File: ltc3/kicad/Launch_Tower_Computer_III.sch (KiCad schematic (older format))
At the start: 0 parts

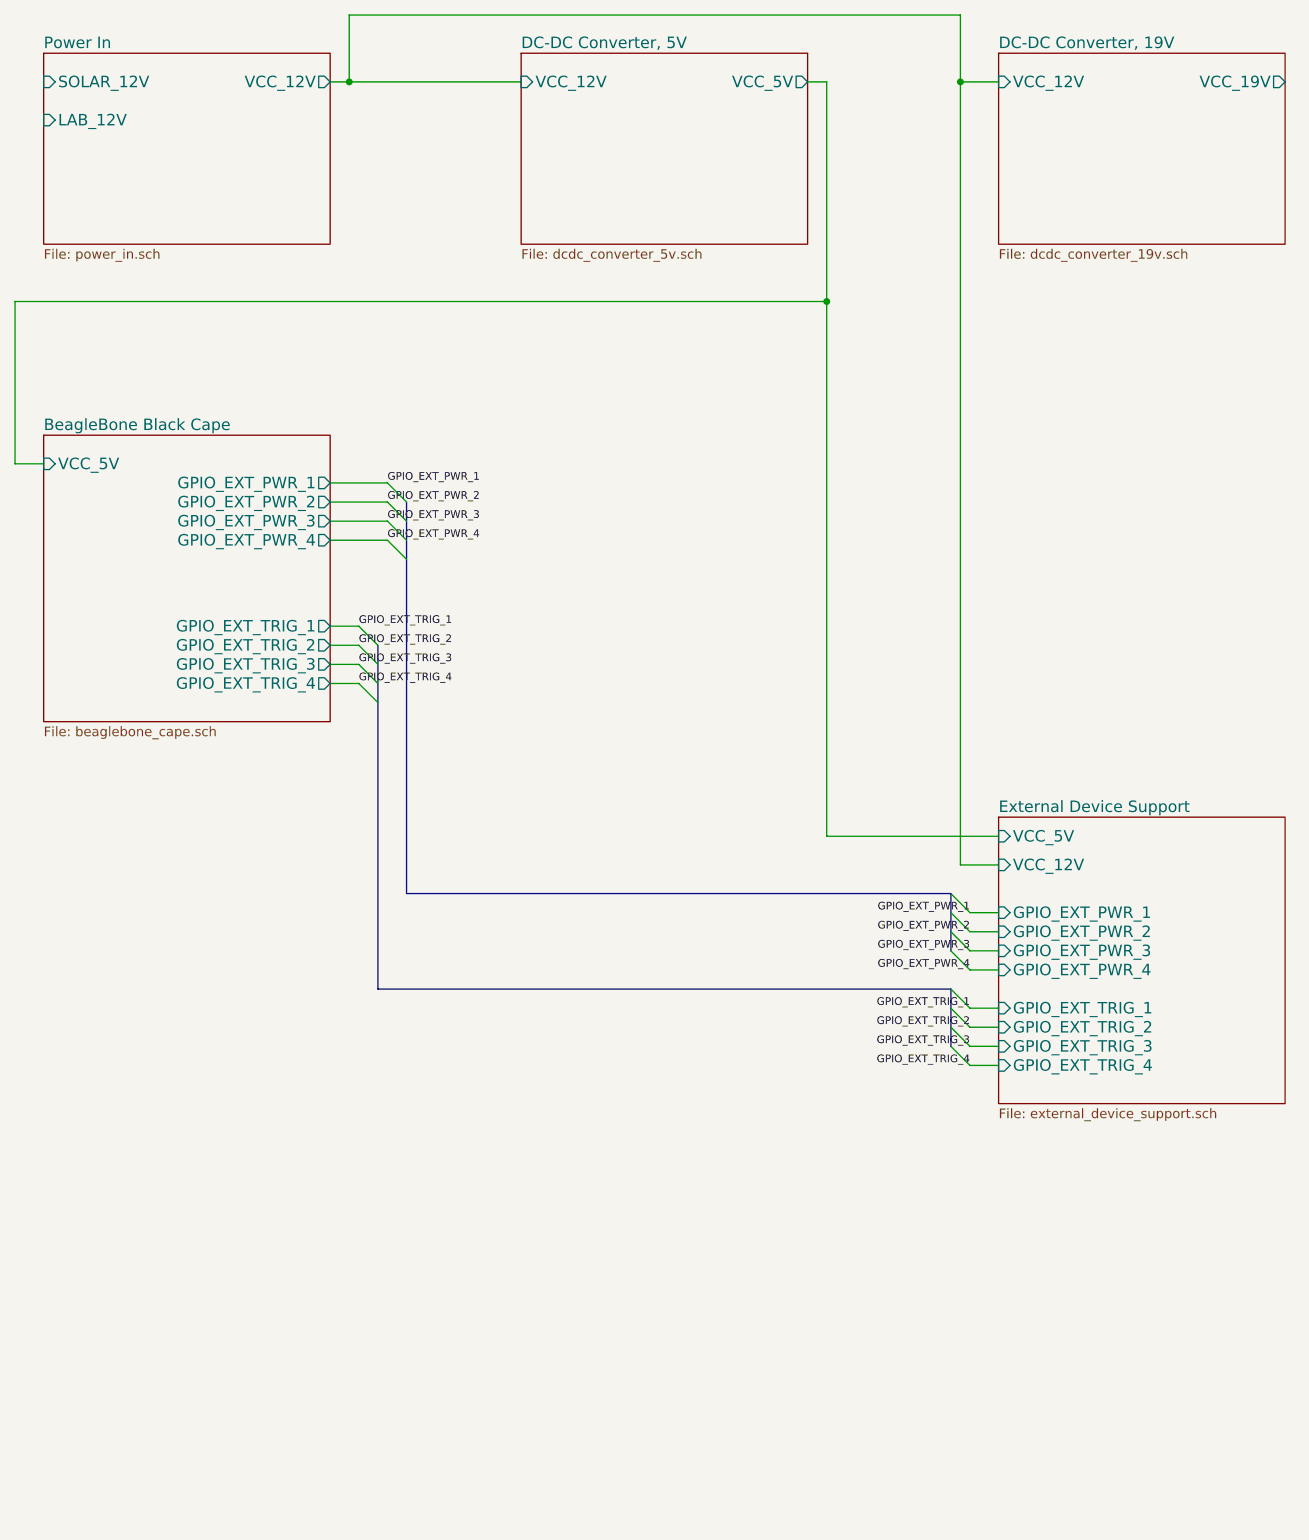
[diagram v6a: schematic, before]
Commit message: Modified LTC3 external device support schematics. 1. Split single sheet into separate power and trigger sheets. 2. Added current-limiting resistor to LED input pin on each    photorelay. 3. Added bleed resistor and filter capacitor across each output    connector.
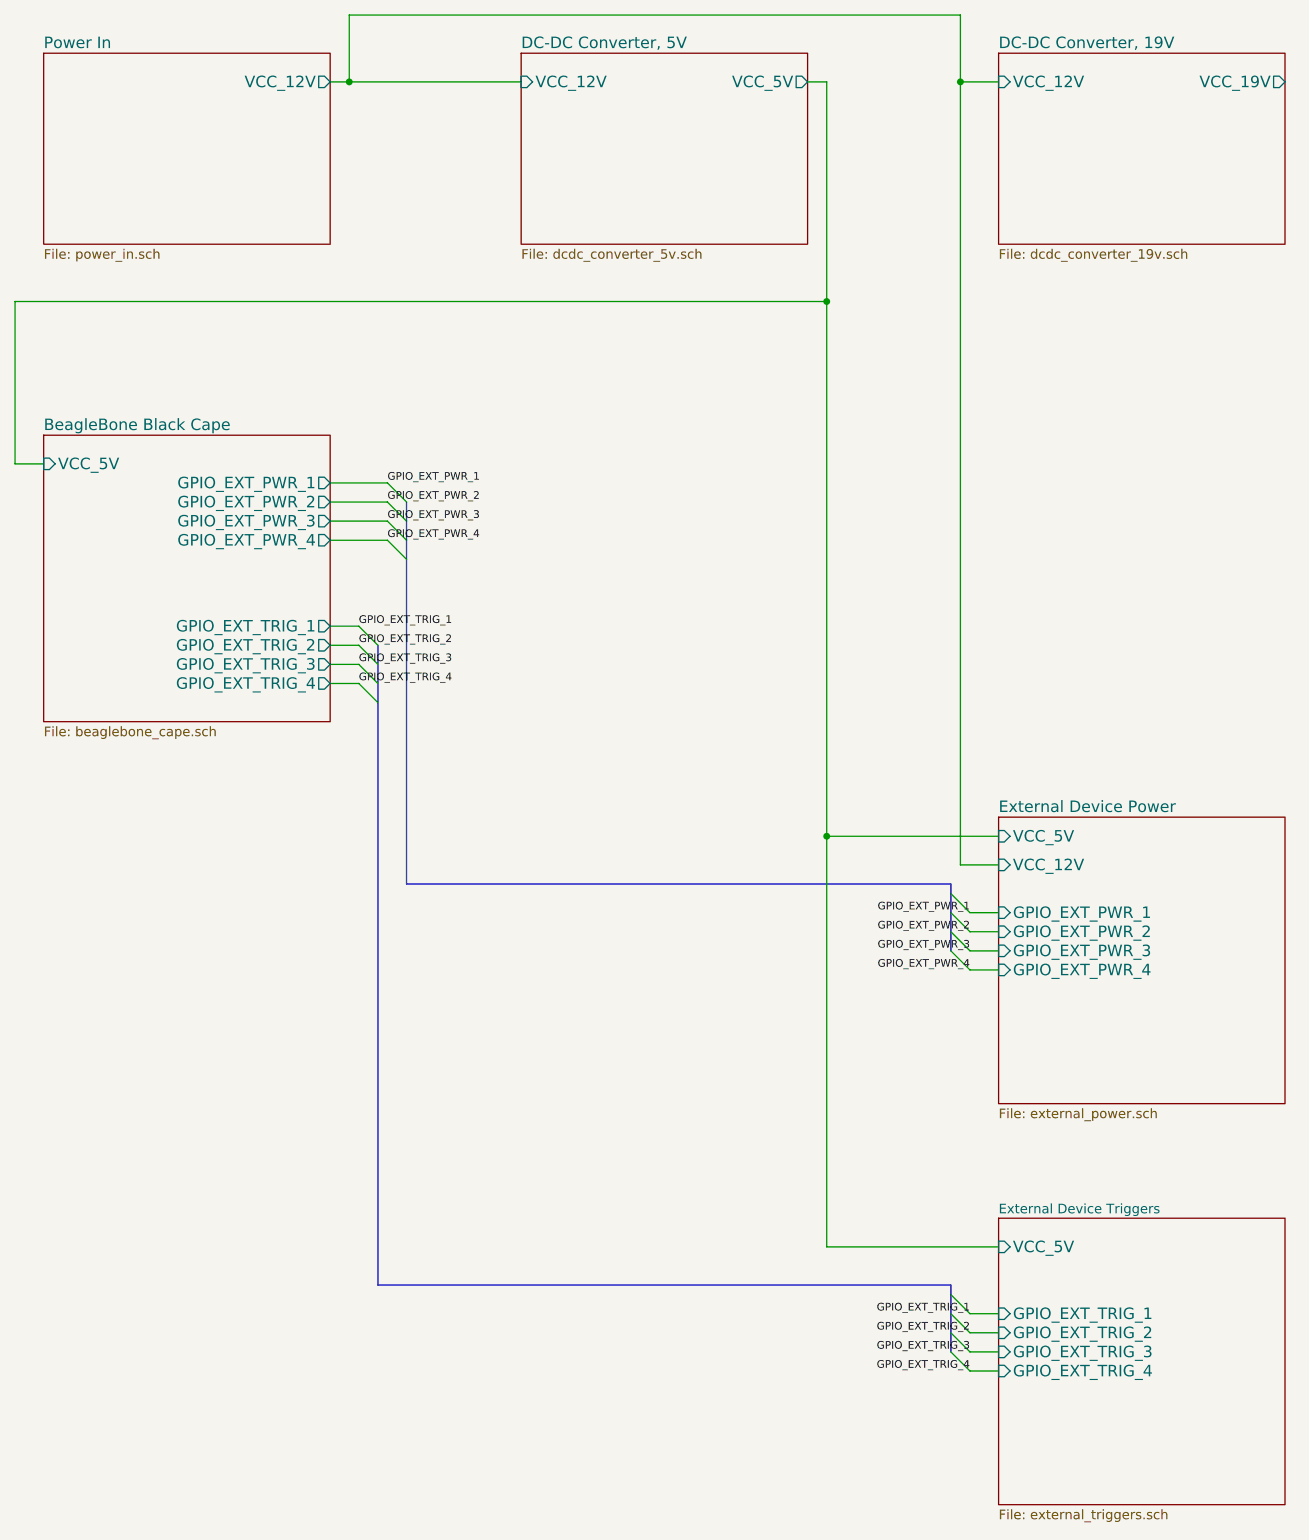
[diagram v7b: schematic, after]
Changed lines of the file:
@@
 $Descr B 17000 11000
 encoding utf-8
-Sheet 1 6
+Sheet 1 7
 Title "Launch Tower Computer III (LTC3)"
-Date "8 apr 2015"
+Date "18 apr 2015"
 Rev "1"
 Comp "Portland State Aerospace Society <http://psas.pdx.edu/>"
@@
 F1 "power_in.sch" 50
 F2 "VCC_12V" O R 2500 1250 60
-F3 "SOLAR_12V" I L 1000 1250 60
-F4 "LAB_12V" I L 1000 1450 60
 $EndSheet
 $Sheet
@@
 	5000 1250 5100 1250
 Wire Wire Line
-	5100 1250 5100 5200
+	5100 1250 5100 7350
 Wire Wire Line
 	5100 2400 850  2400
@@
 F10 "GPIO_EXT_PWR_4" O R 2500 3650 60
 $EndSheet
-$Sheet
-S 6000 5100 1500 1500
-U 551C79BE
-F0 "External Device Support" 60
-F1 "external_device_support.sch" 50
-F2 "VCC_12V" I L 6000 5350 60
-F3 "VCC_5V" I L 6000 5200 60
-F4 "GPIO_EXT_TRIG_1" I L 6000 6100 60
-F5 "GPIO_EXT_TRIG_2" I L 6000 6200 60
-F6 "GPIO_EXT_TRIG_3" I L 6000 6300 60
-F7 "GPIO_EXT_TRIG_4" I L 6000 6400 60
-F8 "GPIO_EXT_PWR_1" I L 6000 5600 60
-F9 "GPIO_EXT_PWR_2" I L 6000 5700 60
-F10 "GPIO_EXT_PWR_4" I L 6000 5900 60
-F11 "GPIO_EXT_PWR_3" I L 6000 5800 60
-$EndSheet
 Wire Wire Line
 	2500 3350 2800 3350
@@
 	6000 5900 5850 5900
 Wire Wire Line
-	6000 6100 5850 6100
-Wire Wire Line
-	6000 6200 5850 6200
-Wire Wire Line
-	6000 6300 5850 6300
-Wire Wire Line
-	6000 6400 5850 6400
+	6000 7700 5850 7700
+Wire Wire Line
+	6000 7800 5850 7800
+Wire Wire Line
+	6000 7900 5850 7900
+Wire Wire Line
+	6000 8000 5850 8000
 Entry Wire Line
 	5750 5500 5850 5600
@@
 	5750 5800 5850 5900
 Entry Wire Line
-	5750 6000 5850 6100
-Entry Wire Line
-	5750 6100 5850 6200
-Entry Wire Line
-	5750 6200 5850 6300
-Entry Wire Line
-	5750 6300 5850 6400
-Wire Bus Line
-	2750 4200 2750 6000
-Wire Bus Line
-	2750 6000 5750 6000
-Wire Bus Line
-	5750 6000 5750 6300
-Wire Bus Line
-	2900 3450 2900 5500
-Wire Bus Line
-	2900 5500 5750 5500
-Wire Bus Line
-	5750 5500 5750 5800
+	5750 7600 5850 7700
+Entry Wire Line
+	5750 7700 5850 7800
+Entry Wire Line
+	5750 7800 5850 7900
+Entry Wire Line
+	5750 7900 5850 8000
+Wire Bus Line
+	5750 7550 5750 7900
+Wire Bus Line
+	5750 5450 5750 5800
 Text Label 2800 3350 0    40   ~ 0
 GPIO_EXT_PWR_1
@@
 Text Label 5850 5900 2    40   ~ 0
 GPIO_EXT_PWR_4
-Text Label 5850 6100 2    40   ~ 0
+Text Label 5850 7700 2    40   ~ 0
 GPIO_EXT_TRIG_1
-Text Label 5850 6200 2    40   ~ 0
+Text Label 5850 7800 2    40   ~ 0
 GPIO_EXT_TRIG_2
-Text Label 5850 6300 2    40   ~ 0
+Text Label 5850 7900 2    40   ~ 0
 GPIO_EXT_TRIG_3
-Text Label 5850 6400 2    40   ~ 0
+Text Label 5850 8000 2    40   ~ 0
 GPIO_EXT_TRIG_4
 Wire Wire Line
 	5800 5350 6000 5350
 Connection ~ 5800 1250
+$Sheet
+S 6000 7200 1500 1500
+U 553268FD
+F0 "External Device Triggers" 50
+F1 "external_triggers.sch" 50
+F2 "GPIO_EXT_TRIG_1" I L 6000 7700 60
+F3 "VCC_5V" I L 6000 7350 60
+F4 "GPIO_EXT_TRIG_2" I L 6000 7800 60
+F5 "GPIO_EXT_TRIG_3" I L 6000 7900 60
+F6 "GPIO_EXT_TRIG_4" I L 6000 8000 60
+$EndSheet
+$Sheet
+S 6000 5100 1500 1500
+U 551C79BE
+F0 "External Device Power" 60
+F1 "external_power.sch" 50
+F2 "VCC_12V" I L 6000 5350 60
+F3 "VCC_5V" I L 6000 5200 60
+F4 "GPIO_EXT_PWR_1" I L 6000 5600 60
+F5 "GPIO_EXT_PWR_2" I L 6000 5700 60
+F6 "GPIO_EXT_PWR_4" I L 6000 5900 60
+F7 "GPIO_EXT_PWR_3" I L 6000 5800 60
+$EndSheet
+Wire Bus Line
+	2750 4200 2750 7550
+Wire Bus Line
+	2750 7550 5750 7550
+Wire Bus Line
+	2900 3450 2900 5450
+Wire Bus Line
+	2900 5450 5750 5450
+Wire Wire Line
+	5100 7350 6000 7350
+Connection ~ 5100 5200
 $EndSCHEMATC

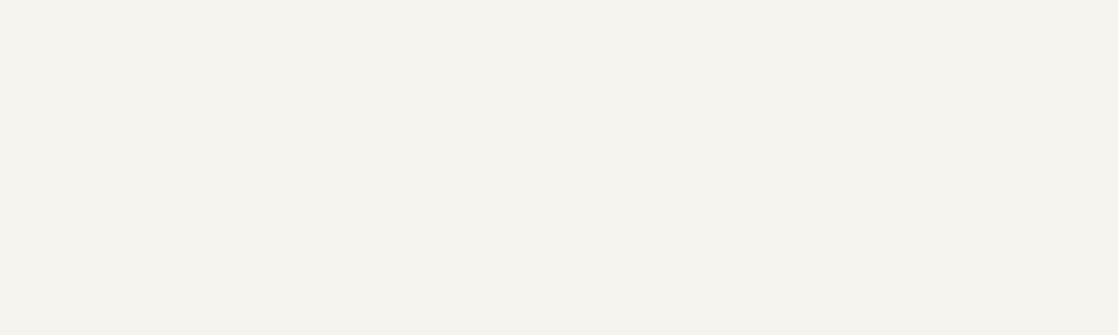
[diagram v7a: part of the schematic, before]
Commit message: Updated datasheet collection.  Added notes to schematic.
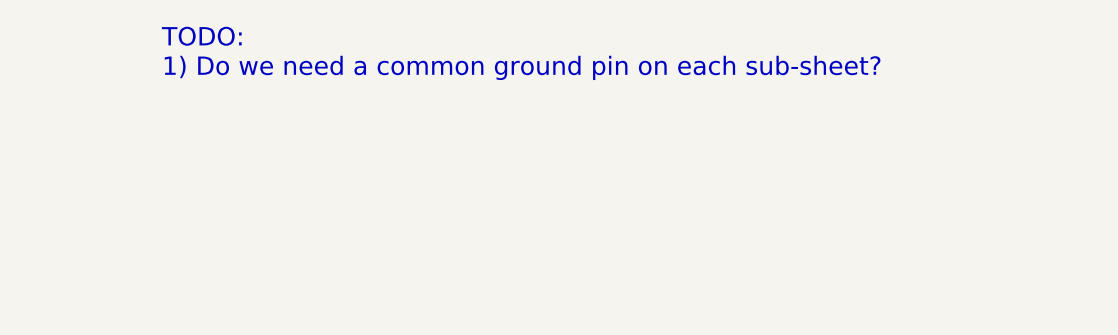
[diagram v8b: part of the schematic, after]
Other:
- note added: "TODO:\n1) Do we need a common ground pin on each sub-sheet?"
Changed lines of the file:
@@
 	5100 7350 6000 7350
 Connection ~ 5100 5200
+Text Notes 12400 1100 0    80   ~ 0
+TODO:\n1) Do we need a common ground pin on each sub-sheet?
 $EndSCHEMATC
